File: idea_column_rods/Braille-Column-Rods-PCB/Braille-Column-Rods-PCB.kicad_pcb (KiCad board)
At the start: 2 copper layers, 95 x 99 mm, 151 parts, among them J1 Conn_01x03, J3 Conn_01x02, J4 Conn_01x08, J5 Screw_Terminal_01x02, J6 Screw_Terminal_01x02, J7 Conn_01x02, M1 Stepper_Motor_bipolar, M10 Motor_DC_With_MP, M11 Motor_DC_With_MP, M12 Motor_DC_With_MP, M2 Stepper_Motor_bipolar, M3 Stepper_Motor_bipolar, M4 Stepper_Motor_bipolar, M5 Stepper_Motor_bipolar, M6 Stepper_Motor_bipolar, M7 Stepper_Motor_bipolar, M8 Stepper_Motor_bipolar, M9 Motor_DC_With_MP, SW1 SW_Push, SW2 SW_Push, U1 DRV8847SPWR, U10 AD116, U11 AD116, U12 AD116, U13 AD116, U14 74HC595, U15 74HC595, U17 MT910xET, U18 MT910xET, U19 MT910xET, U2 DRV8847SPWR, U20 MT910xET, U21 MT910xET, U22 MT910xET, U23 MT910xET, U24 MT910xET, U25 MT910xET, U26 MT910xET, U27 MT910xET, U28 MT910xET, U3 RP2040-Zero, U30 CD74HC4067M, U4 DRV8847SPWR, U5 DRV8847SPWR, U6 DRV8847SPWR, U7 DRV8847SPWR, U8 DRV8847SPWR, U9 DRV8847SPWR

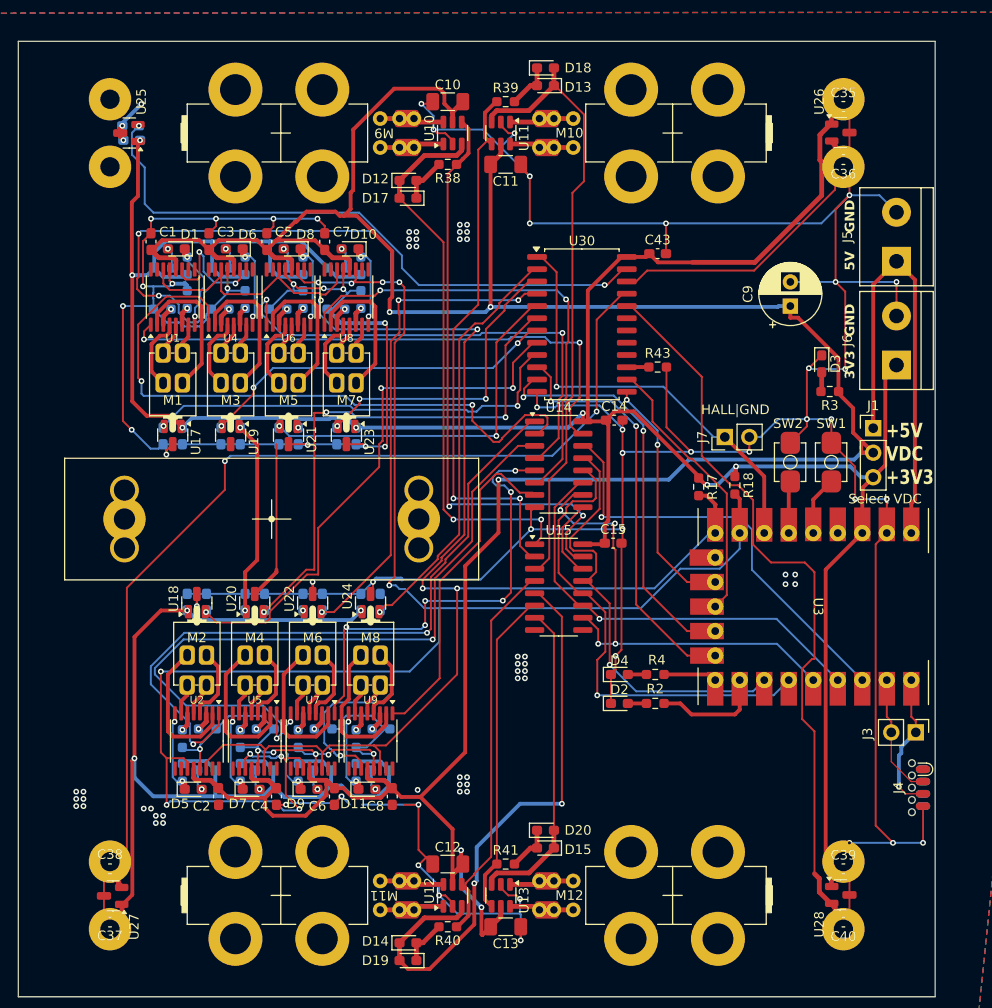
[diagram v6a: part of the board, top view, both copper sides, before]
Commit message: WIP: Reorder the cam bushing and hall sensor
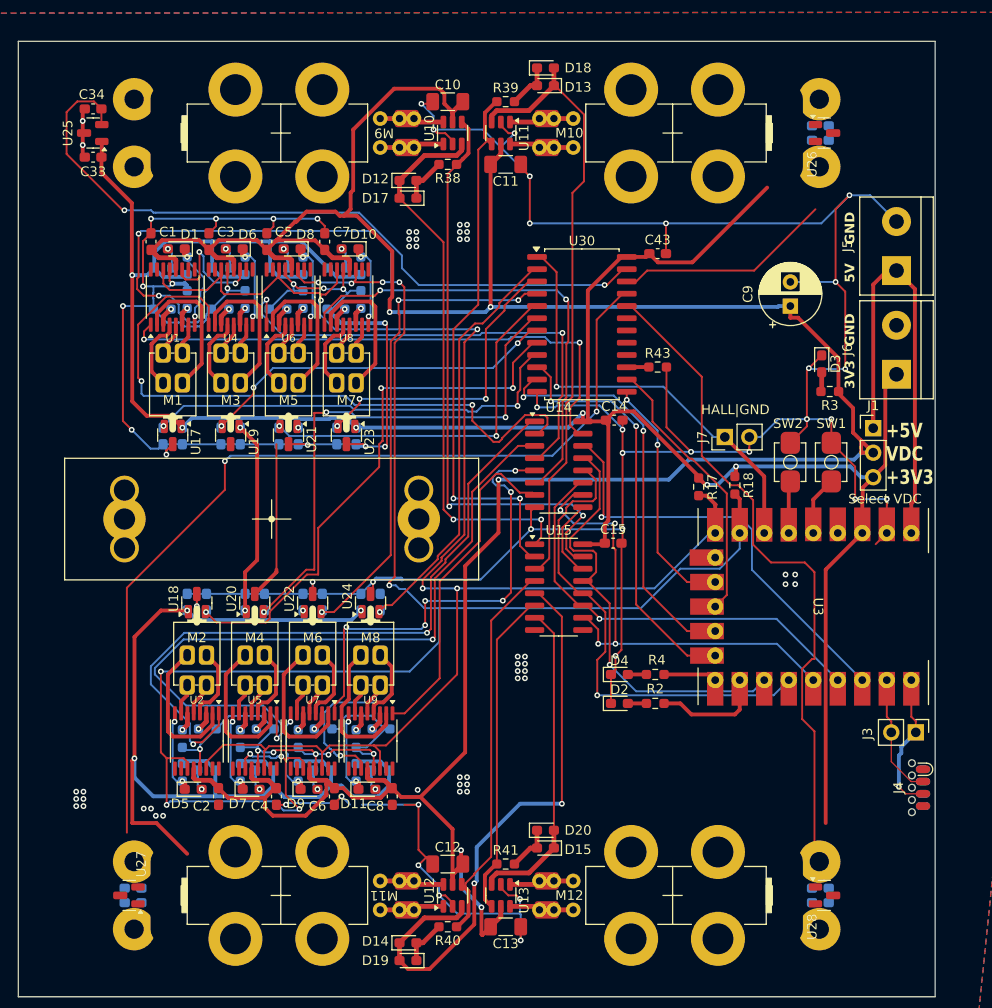
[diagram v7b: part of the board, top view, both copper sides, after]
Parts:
- C33, C34: moved to F.Cu
- C35, C36, C37, C38, C39, C40: moved to B.Cu
- moved C33 4.37 mm to (91.8, 87.5)
- moved C34 4.26 mm to (91.8, 82.5)
- moved U25 3.75 mm to (91.8, 85.0)
- moved C36 3.11 mm to (167.1, 85.7)
- moved C40 3.11 mm to (167.1, 164.7)
- moved C37 3.11 mm to (95.9, 164.8)
- moved C38 3.11 mm to (95.9, 163.2)
- moved C35 3.11 mm to (167.1, 84.2)
- moved C39 3.11 mm to (167.1, 163.2)
- moved U27 1.69 mm to (95.5, 164.0)
- moved U28 1.69 mm to (167.5, 164.0)
- moved U26 1.69 mm to (167.5, 85.0)
- moved J5 0.96 mm to (175.0, 99.2)
- moved J6 0.96 mm to (175.0, 110.0)
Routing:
- net GND: track 606.4 -> 530.2 mm, vias 105 -> 98
- net +3V3: track 420.3 -> 394.2 mm, vias 14 -> 13
- net /Motor_Control/HALL_8: track 64.0 -> 75.5 mm
- net /Motor_Control/HALL_9: track 31.4 -> 22.6 mm
- net /Motor_Control/HALL_11: track 77.5 -> 70.8 mm
- net /Motor_Control/HALL_10: track 103.2 -> 97.1 mm
- net +5V: track 49.9 -> 48.5 mm

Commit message: Complete type 4 rev 1
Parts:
- C35, C36, C37, C38, C39, C40: moved to F.Cu
- moved C37 4.49 mm to (91.8, 166.5)
- moved C38 4.49 mm to (91.8, 161.5)
- moved C35 4.49 mm to (171.2, 82.5)
- moved C36 4.49 mm to (171.2, 87.5)
- moved C39 4.49 mm to (171.2, 161.5)
- moved C40 4.49 mm to (171.2, 166.5)
- moved U26 3.75 mm to (171.2, 85.0)
- moved U27 3.75 mm to (91.8, 164.0)
- moved U28 3.75 mm to (171.2, 164.0)
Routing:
- net +3V3: track 394.2 -> 448.9 mm
- net /Motor_Control/HALL_11: track 70.8 -> 94.4 mm
- net /Motor_Control/HALL_9: track 22.6 -> 31.1 mm
- net /Motor_Control/HALL_10: track 97.1 -> 103.8 mm
- net GND: vias 98 -> 104
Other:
- board text added: "Braille Cam Rod Prototype Type 4, Rev 1 2025-01-06"
